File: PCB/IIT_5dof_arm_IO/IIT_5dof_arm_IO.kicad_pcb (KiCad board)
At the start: 2 copper layers, 60.5 x 0.5 mm, 48 parts, among them J15 Conn_01x03, J16 Conn_01x05, J2 Conn_02x03_Counter_Clockwise, J3 Conn_01x03, J4 Conn_01x04, J5 Conn_01x04, SW10 SW_Push, SW11 SW_Push, SW12 SW_Push, SW13 SW_Push, SW14 SW_Push, SW2 SW_Push, SW4 SW_Push, SW5 SW_Push, SW6 SW_Push, SW7 SW_Push, SW8 SW_Push, SW9 SW_Push, U6 ATmega328P-A, Y1 16MHz

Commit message: Split control board and I/O cards into separate projects
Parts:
- removed BZ1: Buzzer, Connector_Molex:Molex_KK-254_AE-6410-02A_1x02_P2.54mm_Vertical
- removed C10, C6, C7, C9: 100nF, Capacitor_SMD:C_0805_2012Metric_Pad1.18x1.45mm_HandSolder
- removed C2, C3: 22pF, Capacitor_SMD:C_0805_2012Metric_Pad1.18x1.45mm_HandSolder
- removed C4, C5: 1uF, Capacitor_SMD:C_0805_2012Metric_Pad1.18x1.45mm_HandSolder
- removed C8: 4.7uF, Capacitor_SMD:C_1206_3216Metric_Pad1.33x1.80mm_HandSolder
- removed D14: LED, LED_THT:LED_D5.0mm
- removed J15, J3: Conn_01x03, Connector_Molex:Molex_KK-254_AE-6410-03A_1x03_P2.54mm_Vertical
- removed J16: Conn_01x05, Connector_Molex:Molex_KK-254_AE-6410-05A_1x05_P2.54mm_Vertical
- removed J2: Conn_02x03_Counter_Clockwise, Connector_PinHeader_2.54mm:PinHeader_2x03_P2.54mm_Vertical
- removed J4, J5: Conn_01x04, Connector_Molex:Molex_KK-254_AE-6410-04A_1x04_P2.54mm_Vertical
- removed R20, R21, R22, R23, R24, R25, R26, R27, R28, R29, R30, R31, R35: 220, Resistor_SMD:R_0805_2012Metric_Pad1.20x1.40mm_HandSolder
- removed R32, R33, R34, R52: 10k, Resistor_SMD:R_0805_2012Metric_Pad1.20x1.40mm_HandSolder
- removed SW10, SW11, SW12, SW13, SW14, SW2, SW4, SW5, SW6, SW7, SW8, SW9: SW_Push, Connector_Molex:Molex_KK-254_AE-6410-02A_1x02_P2.54mm_Vertical
- removed U6: ATmega328P-A, Package_QFP:TQFP-32_7x7mm_P0.8mm
- removed Y1: 16MHz, Crystal:Crystal_SMD_HC49-SD_HandSoldering
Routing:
- net (no net): track 966.4 -> 0.00 mm, vias 16 -> 0
- removed copper zone on B.Cu, net (none)
- removed copper zone on F.Cu, net (none)
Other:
- board outline removed

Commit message: Organize schematic and generate initi PCB
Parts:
- added BZ1: Buzzer, Connector_Molex:Molex_KK-254_AE-6410-02A_1x02_P2.54mm_Vertical, F.Cu at (148.5, 46.3)
- added C1: 100nF, Capacitor_SMD:C_0805_2012Metric_Pad1.18x1.45mm_HandSolder, F.Cu at (160.5, 82.1)
- added C2: 10nF, Capacitor_SMD:C_0805_2012Metric_Pad1.18x1.45mm_HandSolder, F.Cu at (160.5, 85.2)
- added C3: 10nF, Capacitor_SMD:C_0805_2012Metric_Pad1.18x1.45mm_HandSolder, F.Cu at (160.5, 88.2)
- added C4: 10nF, Capacitor_SMD:C_0805_2012Metric_Pad1.18x1.45mm_HandSolder, F.Cu at (160.5, 91.2)
- added C5: 22pF, Capacitor_SMD:C_0805_2012Metric_Pad1.18x1.45mm_HandSolder, F.Cu at (160.5, 94.2)
- added C6: 22pF, Capacitor_SMD:C_0805_2012Metric_Pad1.18x1.45mm_HandSolder, F.Cu at (160.5, 97.2)
- added C7: 1uF, Capacitor_SMD:C_0805_2012Metric_Pad1.18x1.45mm_HandSolder, F.Cu at (160.5, 100.2)
- added C8: 4.7uF, Capacitor_SMD:C_1206_3216Metric_Pad1.33x1.80mm_HandSolder, F.Cu at (178.9, 104.3)
- added C9: 1uF, Capacitor_SMD:C_0805_2012Metric_Pad1.18x1.45mm_HandSolder, F.Cu at (160.5, 103.2)
- added D13: D, Diode_SMD:D_0805_2012Metric_Pad1.15x1.40mm_HandSolder, F.Cu at (142.9, 91.0)
- added D14: LED, Connector_Molex:Molex_KK-254_AE-6410-02A_1x02_P2.54mm_Vertical, F.Cu at (155.6, 46.3)
- added J1: Conn_01x05, Connector_Molex:Molex_KK-254_AE-6410-05A_1x05_P2.54mm_Vertical, F.Cu at (131.2, 105.0)
- added J10: Conn_01x06, Connector_Molex:Molex_KK-254_AE-6410-06A_1x06_P2.54mm_Vertical, F.Cu at (58.5, 42.1)
- added J11: Conn_01x06, Connector_Molex:Molex_KK-254_AE-6410-06A_1x06_P2.54mm_Vertical, F.Cu at (58.5, 49.9)
- added J12: Conn_01x06, Connector_Molex:Molex_KK-254_AE-6410-06A_1x06_P2.54mm_Vertical, F.Cu at (58.5, 57.8)
- added J13: Conn_01x06, Connector_Molex:Molex_KK-254_AE-6410-06A_1x06_P2.54mm_Vertical, F.Cu at (58.5, 65.6)
- added J2: Conn_01x03, Connector_Molex:Molex_KK-254_AE-6410-03A_1x03_P2.54mm_Vertical, F.Cu at (177.5, 84.6)
- added J3: Conn_02x03_Counter_Clockwise, Connector_PinHeader_2.54mm:PinHeader_2x03_P2.54mm_Vertical, F.Cu at (179.5, 68.2)
- added J4: Conn_01x03, Connector_Molex:Molex_KK-254_AE-6410-03A_1x03_P2.54mm_Vertical, F.Cu at (177.5, 92.4)
- added J5: Conn_01x04, Connector_Molex:Molex_KK-254_AE-6410-04A_1x04_P2.54mm_Vertical, F.Cu at (165.2, 84.6)
- added J6: Conn_01x04, Connector_Molex:Molex_KK-254_AE-6410-04A_1x04_P2.54mm_Vertical, F.Cu at (165.2, 92.4)
- added J7: Conn_02x13_Top_Bottom, Connector_IDC:IDC-Header_2x13_P2.54mm_Vertical, F.Cu at (27.0, 56.9)
- added J8: Conn_01x06, Connector_Molex:Molex_KK-254_AE-6410-06A_1x06_P2.54mm_Vertical, F.Cu at (58.5, 26.4)
- added J9: Conn_01x06, Connector_Molex:Molex_KK-254_AE-6410-06A_1x06_P2.54mm_Vertical, F.Cu at (58.5, 34.2)
- added Q1: 2N7002, Package_TO_SOT_SMD:SOT-23, F.Cu at (179.6, 78.0)
- added R1: 10k, Resistor_SMD:R_0805_2012Metric_Pad1.20x1.40mm_HandSolder, F.Cu at (160.5, 67.4)
- added R10: 220, Resistor_SMD:R_0805_2012Metric_Pad1.20x1.40mm_HandSolder, F.Cu at (165.3, 79.2)
- added R11: 220, Resistor_SMD:R_0805_2012Metric_Pad1.20x1.40mm_HandSolder, F.Cu at (170.0, 67.4)
- added R12: 220, Resistor_SMD:R_0805_2012Metric_Pad1.20x1.40mm_HandSolder, F.Cu at (170.0, 70.3)
- added R13: 220, Resistor_SMD:R_0805_2012Metric_Pad1.20x1.40mm_HandSolder, F.Cu at (170.0, 73.3)
- added R14: 220, Resistor_SMD:R_0805_2012Metric_Pad1.20x1.40mm_HandSolder, F.Cu at (170.0, 76.2)
- added R15: 10k, Resistor_SMD:R_0805_2012Metric_Pad1.20x1.40mm_HandSolder, F.Cu at (170.0, 79.2)
- added R16: 10k, Resistor_SMD:R_0805_2012Metric_Pad1.20x1.40mm_HandSolder, F.Cu at (174.8, 67.4)
- added R17: 160, Resistor_SMD:R_0805_2012Metric_Pad1.20x1.40mm_HandSolder, F.Cu at (174.8, 70.3)
- added R18: 100k, Resistor_SMD:R_0805_2012Metric_Pad1.20x1.40mm_HandSolder, F.Cu at (174.8, 73.3)
- added R19: 160, Resistor_SMD:R_0805_2012Metric_Pad1.20x1.40mm_HandSolder, F.Cu at (174.8, 76.2)
- added R2: 10k, Resistor_SMD:R_0805_2012Metric_Pad1.20x1.40mm_HandSolder, F.Cu at (160.5, 70.3)
- added R20: 220, Resistor_SMD:R_0805_2012Metric_Pad1.20x1.40mm_HandSolder, F.Cu at (174.8, 79.2)
- added R3: 220, Resistor_SMD:R_0805_2012Metric_Pad1.20x1.40mm_HandSolder, F.Cu at (160.5, 73.3)
- added R4: 220, Resistor_SMD:R_0805_2012Metric_Pad1.20x1.40mm_HandSolder, F.Cu at (160.5, 76.2)
- added R5: 220, Resistor_SMD:R_0805_2012Metric_Pad1.20x1.40mm_HandSolder, F.Cu at (160.5, 79.2)
- added R6: 220, Resistor_SMD:R_0805_2012Metric_Pad1.20x1.40mm_HandSolder, F.Cu at (165.3, 67.4)
- added R7: 220, Resistor_SMD:R_0805_2012Metric_Pad1.20x1.40mm_HandSolder, F.Cu at (165.3, 70.3)
- added R8: 220, Resistor_SMD:R_0805_2012Metric_Pad1.20x1.40mm_HandSolder, F.Cu at (165.3, 73.3)
- added R9: 220, Resistor_SMD:R_0805_2012Metric_Pad1.20x1.40mm_HandSolder, F.Cu at (165.3, 76.2)
- added SW1: SW_Push, Connector_Molex:Molex_KK-254_AE-6410-02A_1x02_P2.54mm_Vertical, F.Cu at (162.7, 46.3)
- added SW10: SW_Push, Connector_Molex:Molex_KK-254_AE-6410-02A_1x02_P2.54mm_Vertical, F.Cu at (177.0, 54.1)
- added SW11: SW_Push, Connector_Molex:Molex_KK-254_AE-6410-02A_1x02_P2.54mm_Vertical, F.Cu at (148.5, 62.0)
- added SW12: SW_Push, Connector_Molex:Molex_KK-254_AE-6410-02A_1x02_P2.54mm_Vertical, F.Cu at (155.6, 62.0)
- added SW13: SW_Push, Connector_Molex:Molex_KK-254_AE-6410-02A_1x02_P2.54mm_Vertical, F.Cu at (162.7, 62.0)
- added SW14: SW_Push, Connector_Molex:Molex_KK-254_AE-6410-02A_1x02_P2.54mm_Vertical, F.Cu at (169.8, 62.0)
- added SW2: SW_Push, Connector_Molex:Molex_KK-254_AE-6410-02A_1x02_P2.54mm_Vertical, F.Cu at (169.8, 46.3)
- added SW3: SW_Push, Connector_Molex:Molex_KK-254_AE-6410-02A_1x02_P2.54mm_Vertical, F.Cu at (177.0, 46.3)
- added SW4: SW_Push, Connector_Molex:Molex_KK-254_AE-6410-02A_1x02_P2.54mm_Vertical, F.Cu at (148.5, 54.1)
- added SW5: SW_Push, Connector_Molex:Molex_KK-254_AE-6410-02A_1x02_P2.54mm_Vertical, F.Cu at (155.6, 54.1)
- added SW6: SW_Push, Connector_Molex:Molex_KK-254_AE-6410-02A_1x02_P2.54mm_Vertical, F.Cu at (162.7, 54.1)
- added SW8: SW_Push, Button_Switch_SMD:SW_SPST_FSMSM, F.Cu at (169.4, 105.1)
- added SW9: SW_Push, Connector_Molex:Molex_KK-254_AE-6410-02A_1x02_P2.54mm_Vertical, F.Cu at (169.8, 54.1)
- added U1: ATmega328P-A, Package_QFP:TQFP-32_7x7mm_P0.8mm, F.Cu at (134.7, 95.3)
- added Y1: 16MHz, Crystal:Crystal_SMD_HC49-SD_HandSoldering, F.Cu at (173.7, 99.5)
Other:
- board outline added: 100 x 100 mm

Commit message: PCB layout
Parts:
- removed J10, J11, J12, J13, J8, J9: Conn_01x06, Connector_Molex:Molex_KK-254_AE-6410-06A_1x06_P2.54mm_Vertical
- removed J7: Conn_02x13_Top_Bottom, Connector_IDC:IDC-Header_2x13_P2.54mm_Vertical
- added C10: 0.33uF, Capacitor_SMD:C_0805_2012Metric_Pad1.18x1.45mm_HandSolder, F.Cu at (91.4, 52.3)
- added C11: 0.047uF, Capacitor_SMD:C_0805_2012Metric_Pad1.18x1.45mm_HandSolder, F.Cu at (95.7, 52.3)
- added C12: 0.1uF, Capacitor_SMD:C_0805_2012Metric_Pad1.18x1.45mm_HandSolder, B.Cu at (95.7, 70.8)
- added C13: 0.33uF, Capacitor_SMD:C_0805_2012Metric_Pad1.18x1.45mm_HandSolder, B.Cu at (94.5, 52.4)
- added C14: 0.33uF, Capacitor_SMD:C_0805_2012Metric_Pad1.18x1.45mm_HandSolder, F.Cu at (87.9, 52.1)
- added C15: 10nF, Capacitor_SMD:C_0805_2012Metric_Pad1.18x1.45mm_HandSolder, B.Cu at (104.1, 34.3)
- added C16: 10nF, Capacitor_SMD:C_0805_2012Metric_Pad1.18x1.45mm_HandSolder, B.Cu at (92.5, 34.3)
- added C17: 10nF, Capacitor_SMD:C_0805_2012Metric_Pad1.18x1.45mm_HandSolder, B.Cu at (80.5, 34.0)
- added C18: 10nF, Capacitor_SMD:C_0805_2012Metric_Pad1.18x1.45mm_HandSolder, B.Cu at (68.1, 34.0)
- added C19: 10nF, Capacitor_SMD:C_0805_2012Metric_Pad1.18x1.45mm_HandSolder, B.Cu at (55.5, 34.3)
- added C20: 10nF, Capacitor_SMD:C_0805_2012Metric_Pad1.18x1.45mm_HandSolder, B.Cu at (59.4, 86.1)
- added C21: 10nF, Capacitor_SMD:C_0805_2012Metric_Pad1.18x1.45mm_HandSolder, B.Cu at (64.3, 90.5)
- added C22: 10nF, Capacitor_SMD:C_0805_2012Metric_Pad1.18x1.45mm_HandSolder, B.Cu at (84.6, 90.5)
- added C23: 10nF, Capacitor_SMD:C_0805_2012Metric_Pad1.18x1.45mm_HandSolder, B.Cu at (96.7, 90.5)
- added C24: 10nF, Capacitor_SMD:C_0805_2012Metric_Pad1.18x1.45mm_HandSolder, B.Cu at (108.6, 90.5)
- added C25: 10nF, Capacitor_SMD:C_0805_2012Metric_Pad1.18x1.45mm_HandSolder, F.Cu at (32.1, 38.6)
- added C26: 10nF, Capacitor_SMD:C_0805_2012Metric_Pad1.18x1.45mm_HandSolder, F.Cu at (34.3, 86.1)
- added D1: LED, Connector_Molex:Molex_KK-254_AE-6410-02A_1x02_P2.54mm_Vertical, F.Cu at (99.3, 25.1)
- added D10: LED, Connector_Molex:Molex_KK-254_AE-6410-02A_1x02_P2.54mm_Vertical, F.Cu at (68.8, 99.5)
- added D11: LED, Connector_Molex:Molex_KK-254_AE-6410-02A_1x02_P2.54mm_Vertical, F.Cu at (53.7, 99.5)
- added D12: LED, Connector_Molex:Molex_KK-254_AE-6410-02A_1x02_P2.54mm_Vertical, F.Cu at (41.4, 99.5)
- added D15: SMAJ12A, Diode_SMD:D_SMA, B.Cu at (100.2, 71.8)
- added D16: SMAJ12A, Diode_SMD:D_SMA, F.Cu at (104.4, 71.7)
- added D17: SMAJ12A, Diode_SMD:D_SMA, F.Cu at (104.2, 63.8)
- added D2: LED, Connector_Molex:Molex_KK-254_AE-6410-02A_1x02_P2.54mm_Vertical, F.Cu at (87.3, 25.1)
- added D3: LED, Connector_Molex:Molex_KK-254_AE-6410-02A_1x02_P2.54mm_Vertical, F.Cu at (75.7, 25.1)
- added D4: LED, Connector_Molex:Molex_KK-254_AE-6410-02A_1x02_P2.54mm_Vertical, F.Cu at (63.4, 25.1)
- added D5: LED, Connector_Molex:Molex_KK-254_AE-6410-02A_1x02_P2.54mm_Vertical, F.Cu at (50.8, 25.1)
- added D6: LED, Connector_Molex:Molex_KK-254_AE-6410-02A_1x02_P2.54mm_Vertical, F.Cu at (37.0, 25.0)
- added D7: LED, Connector_Molex:Molex_KK-254_AE-6410-02A_1x02_P2.54mm_Vertical, F.Cu at (104.0, 99.5)
- added D8: LED, Connector_Molex:Molex_KK-254_AE-6410-02A_1x02_P2.54mm_Vertical, F.Cu at (92.0, 99.5)
- added D9: LED, Connector_Molex:Molex_KK-254_AE-6410-02A_1x02_P2.54mm_Vertical, F.Cu at (80.0, 99.5)
- added F1: 1812L050PR, IIT_5dof_arm_IO:1812L050PR__1.78mm_3.15mm_3.45mm, B.Cu at (104.5, 72.4)
- added G***: LOGO, IIT_5dof_arm:IIT_logo_15x15mm, F.Cu at (42.2, 71.6)
- added H1: MountingHole, MountingHole:MountingHole_3.2mm_M3, F.Cu at (24.0, 24.0)
- added H2: MountingHole, MountingHole:MountingHole_3.2mm_M3, F.Cu at (116.0, 24.0)
- added H3: MountingHole, MountingHole:MountingHole_3.2mm_M3, F.Cu at (24.0, 101.0)
- added H4: MountingHole, MountingHole:MountingHole_3.2mm_M3, F.Cu at (116.0, 101.0)
- added Q2: 2N7002, Package_TO_SOT_SMD:SOT-23, F.Cu at (37.1, 33.4)
- added Q3: 2N7002, Package_TO_SOT_SMD:SOT-23, B.Cu at (53.6, 91.2)
- added Q4: 2N7002, Package_TO_SOT_SMD:SOT-23, F.Cu at (41.3, 91.2)
- added R21: 4.7k, Resistor_SMD:R_0805_2012Metric_Pad1.20x1.40mm_HandSolder, B.Cu at (90.1, 67.9)
- added R22: 4.7k, Resistor_SMD:R_0805_2012Metric_Pad1.20x1.40mm_HandSolder, B.Cu at (90.1, 64.4)
- added R23: 10k, Resistor_SMD:R_0805_2012Metric_Pad1.20x1.40mm_HandSolder, F.Cu at (29.5, 50.6)
- added R24: 10k, Resistor_SMD:R_0805_2012Metric_Pad1.20x1.40mm_HandSolder, B.Cu at (104.1, 29.6)
- added R25: 10k, Resistor_SMD:R_0805_2012Metric_Pad1.20x1.40mm_HandSolder, B.Cu at (92.5, 29.6)
- added R26: 10k, Resistor_SMD:R_0805_2012Metric_Pad1.20x1.40mm_HandSolder, B.Cu at (80.5, 29.4)
- added R27: 10k, Resistor_SMD:R_0805_2012Metric_Pad1.20x1.40mm_HandSolder, B.Cu at (68.1, 29.5)
- added R28: 10k, Resistor_SMD:R_0805_2012Metric_Pad1.20x1.40mm_HandSolder, B.Cu at (55.5, 29.7)
- added R29: 10k, Resistor_SMD:R_0805_2012Metric_Pad1.20x1.40mm_HandSolder, F.Cu at (33.2, 29.3)
- added R31: 10k, Resistor_SMD:R_0805_2012Metric_Pad1.20x1.40mm_HandSolder, B.Cu at (108.6, 95.0)
- added R32: 10k, Resistor_SMD:R_0805_2012Metric_Pad1.20x1.40mm_HandSolder, B.Cu at (96.7, 95.0)
- added R33: 10k, Resistor_SMD:R_0805_2012Metric_Pad1.20x1.40mm_HandSolder, B.Cu at (84.6, 95.0)
- added R34: 10k, Resistor_SMD:R_0805_2012Metric_Pad1.20x1.40mm_HandSolder, B.Cu at (50.2, 95.5)
- added R35: 10k, Resistor_SMD:R_0805_2012Metric_Pad1.20x1.40mm_HandSolder, F.Cu at (45.3, 95.5)
- added R37: 10k, Resistor_SMD:R_0805_2012Metric_Pad1.20x1.40mm_HandSolder, B.Cu at (64.3, 95.0)
- added SW15: SW_SPDT, Connector_PinHeader_2.54mm:PinHeader_1x03_P2.54mm_Vertical, F.Cu at (25.0, 47.1)
- added U2: MAX3232, Package_SO:SOIC-16W_5.3x10.2mm_P1.27mm, F.Cu at (91.3, 60.2)
- C4, D13, Q1, R1, R13, R17, R18, R20: moved to B.Cu
- J6: value Conn_01x04 -> DE9_Plug_MountingHoles; footprint Connector_Molex:Molex_KK-254_AE-6410-04A_1x04_P2.54mm_Vertical -> Connector_Dsub:DSUB-9_Male_Horizontal_P2.77x2.84mm_EdgePinOffset7.70mm_Housed_MountingHolesOffset9.12mm
- moved J3 150.1 mm to (29.6, 76.2), turned to -90 degrees
- moved SW8 150.0 mm to (25.1, 64.4), turned to 90 degrees
- moved R19 140.5 mm to (35.5, 57.3), turned to -90 degrees
- moved R15 139.7 mm to (30.7, 68.9)
- moved R8 135.6 mm to (37.0, 29.4), turned to -90 degrees
- moved Q1 132.5 mm to (48.0, 62.6), turned to 180 degrees
- moved SW14 131.9 mm to (40.3, 87.1), turned to 90 degrees
- moved R14 130.2 mm to (41.3, 95.5), turned to 90 degrees
- moved SW6 125.5 mm to (38.0, 40.0), turned to 90 degrees
- moved J2 123.4 mm to (54.5, 73.9), turned to -90 degrees
- moved R18 122.7 mm to (52.5, 62.8), turned to -90 degrees
- moved R7 121.6 mm to (50.9, 29.1), turned to -90 degrees
- moved Y1 120.6 mm to (64.6, 48.1)
- moved R17 118.8 mm to (56.3, 61.9), turned to 180 degrees
- moved R13 118.4 mm to (53.7, 95.5), turned to 90 degrees
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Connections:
- J3 pad 1: /UIPanel_BUTT5A__UIPanel_Prog_MISO -> /UIPanel_BUTT6A__UIPanel_Prog_MOSI
- J3 pad 2: /UIPanel_BUTT6A__UIPanel_Prog_SCK -> /UIPanel_BUTT6B__UIPanel_Prog_MISO
- J3 pad 4: UIPanel_GND -> /UIPanel_BUTT5B__UIPanel_Prog_SCK
- J3 pad 5: /UIPanel_BUTT4A__UIPanel_Prog_MOSI -> UIPanel_+5V
- J3 pad 6: UIPanel_+5V -> UIPanel_GND
- J6 pad 1: UIPanel_+5V -> Net-(F1-Pad1)
- J6 pad 2: /UIPanel_RX -> /RS232_RX
- J6 pad 3: /UIPanel_TX -> /RS232_TX
- J6 pad 4: UIPanel_GND -> unconnected-(J6-Pad4)
- R10 pad 1: /UIPanel_BUTT2B -> Net-(D8-K)
- R10 pad 2: UIPanel_GND -> /UIPanel_BUTT2B
- R11 pad 1: /UIPanel_BUTT3B -> Net-(D9-K)
- R11 pad 2: UIPanel_GND -> /UIPanel_BUTT3B
- R12 pad 1: /UIPanel_BUTT4B -> Net-(D10-K)
- R12 pad 2: UIPanel_GND -> /UIPanel_BUTT4B
- R13 pad 1: /UIPanel_BUTT5B -> Net-(D11-K)
- R13 pad 2: UIPanel_GND -> Net-(Q3-D)
- R14 pad 1: /UIPanel_BUTT6B -> Net-(D12-K)
- R14 pad 2: UIPanel_GND -> Net-(Q4-D)
- R3 pad 1: UIPanel_GND -> Net-(D1-K)
- R4 pad 1: UIPanel_GND -> Net-(D2-K)
- R5 pad 1: UIPanel_GND -> Net-(D3-K)
- R6 pad 1: UIPanel_GND -> Net-(D4-K)
- R6 pad 2: /UIPanel_BUTT4A__UIPanel_Prog_MOSI -> /UIPanel_BUTT4A
- R7 pad 1: UIPanel_GND -> Net-(D5-K)
- R7 pad 2: /UIPanel_BUTT5A__UIPanel_Prog_MISO -> /UIPanel_BUTT5A
- R8 pad 1: UIPanel_GND -> Net-(D6-K)
- R8 pad 2: /UIPanel_BUTT6A__UIPanel_Prog_SCK -> Net-(Q2-D)
- R9 pad 1: /UIPanel_BUTT1B -> Net-(D7-K)
- R9 pad 2: UIPanel_GND -> /UIPanel_BUTT1B
- SW1 pad 1: Net-(SW1-Pad1) -> UIPanel_GND
- SW10 pad 1: Net-(SW10-Pad1) -> /UIPanel_BUTT2B
- SW10 pad 2: /UIPanel_BUTT2B -> UIPanel_GND
- SW11 pad 1: Net-(SW11-Pad1) -> /UIPanel_BUTT3B
- SW11 pad 2: /UIPanel_BUTT3B -> UIPanel_GND
- SW12 pad 1: Net-(SW12-Pad1) -> /UIPanel_BUTT4B
- SW12 pad 2: /UIPanel_BUTT4B -> UIPanel_GND
- SW13 pad 1: Net-(SW13-Pad1) -> /UIPanel_BUTT5B__UIPanel_Prog_SCK
- SW13 pad 2: /UIPanel_BUTT5B -> UIPanel_GND
- SW14 pad 1: Net-(SW14-Pad1) -> /UIPanel_BUTT6B__UIPanel_Prog_MISO
- SW14 pad 2: /UIPanel_BUTT6B -> UIPanel_GND
- SW2 pad 1: Net-(SW2-Pad1) -> UIPanel_GND
- SW3 pad 1: Net-(SW3-Pad1) -> UIPanel_GND
- SW4 pad 1: Net-(SW4-Pad1) -> UIPanel_GND
- SW4 pad 2: /UIPanel_BUTT4A__UIPanel_Prog_MOSI -> /UIPanel_BUTT4A
- SW5 pad 1: Net-(SW5-Pad1) -> UIPanel_GND
- SW5 pad 2: /UIPanel_BUTT5A__UIPanel_Prog_MISO -> /UIPanel_BUTT5A
- SW6 pad 1: Net-(SW6-Pad1) -> UIPanel_GND
- SW6 pad 2: /UIPanel_BUTT6A__UIPanel_Prog_SCK -> /UIPanel_BUTT6A__UIPanel_Prog_MOSI
- SW9 pad 1: Net-(SW9-Pad1) -> /UIPanel_BUTT1B
- SW9 pad 2: /UIPanel_BUTT1B -> UIPanel_GND
- U1 pad 10: /UIPanel_Enc_BUTT -> /UIPanel_BUTT2A
- U1 pad 11: /UIPanel_Buzz -> /UIPanel_BUTT3A
- U1 pad 12: /UIPanel_BUTT1A -> /UIPanel_BUTT4A
- U1 pad 13: /UIPanel_BUTT2A -> /UIPanel_BUTT5A
- U1 pad 14: /UIPanel_BUTT3A -> /UIPanel_Buzz
- U1 pad 15: /UIPanel_BUTT4A__UIPanel_Prog_MOSI -> /UIPanel_BUTT6A__UIPanel_Prog_MOSI
- U1 pad 16: /UIPanel_BUTT5A__UIPanel_Prog_MISO -> /UIPanel_BUTT6B__UIPanel_Prog_MISO
- U1 pad 17: /UIPanel_BUTT6A__UIPanel_Prog_SCK -> /UIPanel_BUTT5B__UIPanel_Prog_SCK
- U1 pad 2: /UIPanel_BUTT5B -> /UIPanel_Enc_BUTT
- U1 pad 23: /UIPanel_BUTT1B -> /UIPanel_BUTT4B
- U1 pad 24: /UIPanel_BUTT2B -> /UIPanel_BUTT3B
- U1 pad 25: /UIPanel_BUTT3B -> /UIPanel_BUTT2B
- U1 pad 26: /UIPanel_BUTT4B -> /UIPanel_BUTT1B
- U1 pad 9: /UIPanel_BUTT6B -> /UIPanel_BUTT1A
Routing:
- net UIPanel_+5V: track 0.00 -> 483.6 mm, vias 0 -> 2
- net /PROG_SW: track 0.00 -> 90.5 mm, vias 0 -> 2
- net /UIPanel_BUTT1A: track 0.00 -> 84.1 mm
- net /UIPanel_BUTT6A__UIPanel_Prog_MOSI: track 0.00 -> 81.2 mm
- net /UIPanel_BUTT2A: track 0.00 -> 74.1 mm
- net /UIPanel_BUTT5B__UIPanel_Prog_SCK: track 0.00 -> 67.6 mm
- net /UIPanel_BUTT3A: track 0.00 -> 64.1 mm
- net /UIPanel_BUTT6B__UIPanel_Prog_MISO: track 0.00 -> 61.8 mm, vias 0 -> 1
- net /UIPanel_reset: track 0.00 -> 60.0 mm, vias 0 -> 2
- net /UIPanel_Enc_BUTT: track 0.00 -> 58.1 mm
- net /UIPanel_BUTT1B: track 0.00 -> 57.8 mm
- net /UIPanel_BUTT4A: track 0.00 -> 53.5 mm
- net /UIPanel_BUTT5A: track 0.00 -> 51.1 mm
- net /UIPanel_Enc_A: track 0.00 -> 50.2 mm
- net /UIPanel_BUTT2B: track 0.00 -> 49.6 mm
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- added copper zone on B.Cu, net UIPanel_GND
- added copper zone on F.Cu, net UIPanel_GND
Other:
- board size 100 x 100 mm -> 100 x 85 mm
- board text added: "+"
- board text added: "+5V"
- board text added: "A1"
- board text added: "A2"
- board text added: "BUTT"
- board text added: "ChA"
- board text added: "ChB"
- board text added: "GND"
- board text added: "Kalm & Mürb Teach-robot Wired remote control v1.0 András Izsó 2024"
- board text added: "MISO"
- board text added: "MOSI"
- board text added: "RESET"
- board text added: "RS232 (DTE): 1: +5V 6: X 2: RX 7: X 3: TX 8: X 4: X 9: X 5: GND"
- board text added: "SCK"
- board text added: "SCL"
- board text added: "SDA"

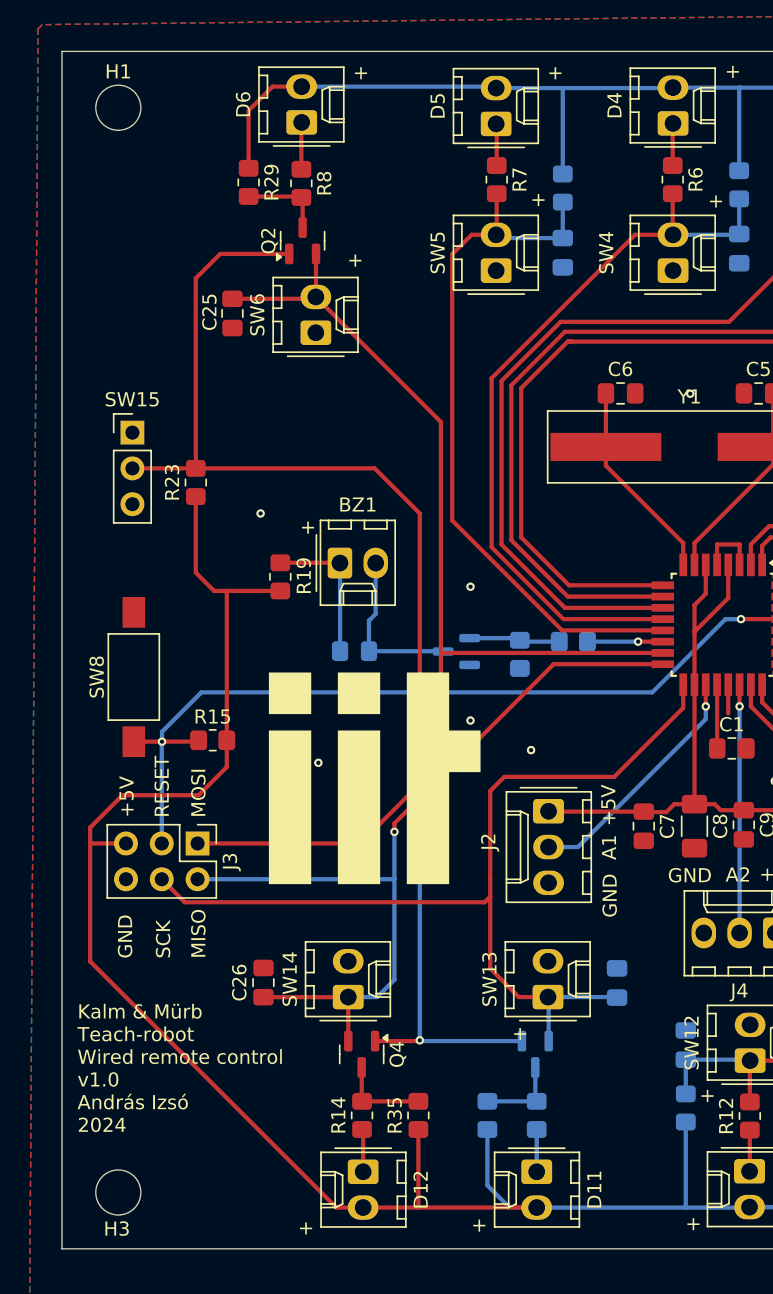
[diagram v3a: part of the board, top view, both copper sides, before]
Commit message: Fix SMAJ value, program pullup switch
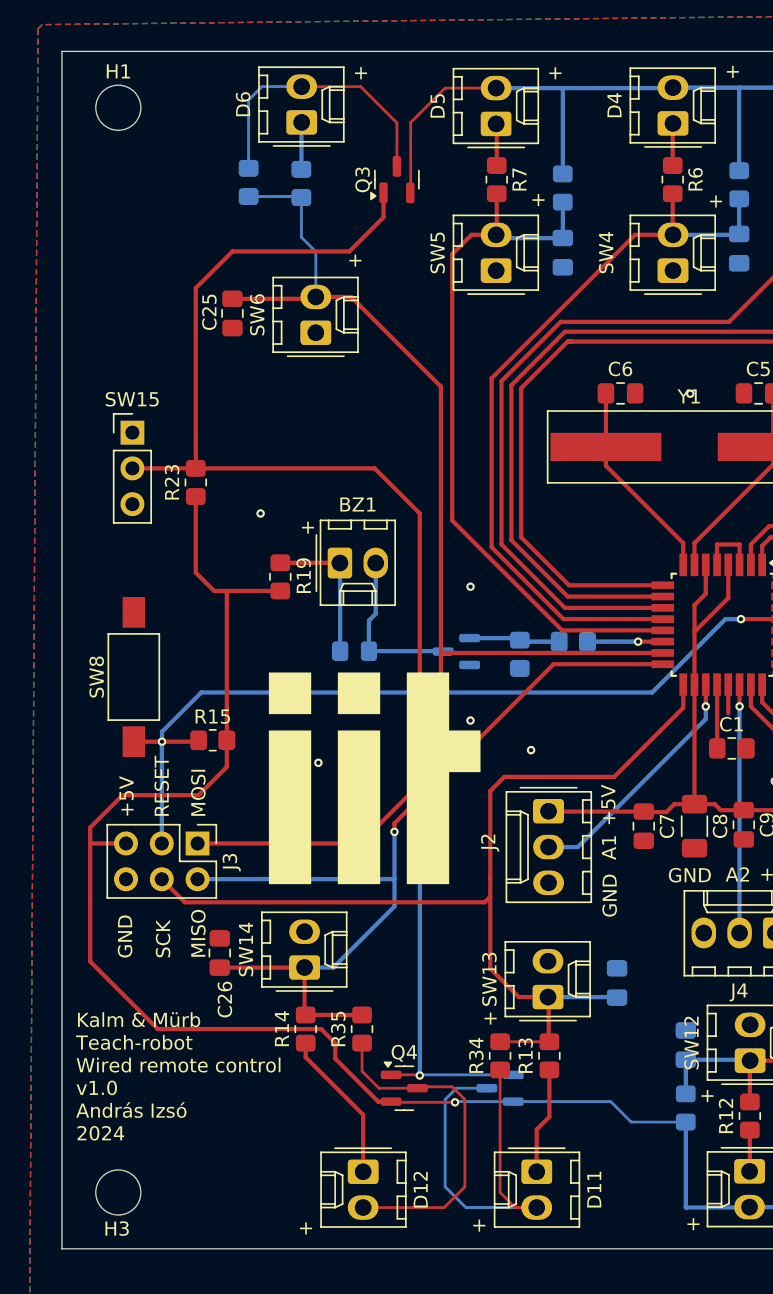
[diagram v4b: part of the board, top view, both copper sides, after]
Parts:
- D15: value SMAJ12A -> SMAJ5.0A
- Q2: value 2N7002 -> BSS84; moved to B.Cu
- Q3: value 2N7002 -> BSS84; moved to F.Cu
- Q4: value 2N7002 -> BSS84
- R13, R34: moved to F.Cu
- R29, R8: moved to B.Cu
- moved Q3 62.9 mm to (43.8, 29.1), turned to 90 degrees
- moved Q2 61.8 mm to (51.1, 93.6), turned to 180 degrees
- moved R14 7.32 mm to (37.3, 89.4)
- moved R35 7.32 mm to (41.3, 89.4)
- moved R13 4.32 mm to (54.6, 91.3)
- moved R34 4.32 mm to (51.1, 91.3)
- moved Q4 3.87 mm to (44.3, 93.6), turned to 0 degrees
- moved SW14 3.74 mm to (37.2, 85.0)
- moved C26 3.74 mm to (31.2, 84.0)
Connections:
- D11 pad 2: UIPanel_+5V -> Net-(D11-A)
- D12 pad 2: UIPanel_+5V -> Net-(D12-A)
- D6 pad 2: UIPanel_+5V -> Net-(D6-A)
- Q2 pad 2: /UIPanel_BUTT6A__UIPanel_Prog_MOSI -> UIPanel_+5V
- Q2 pad 3: Net-(Q2-D) -> Net-(D11-A)
- Q3 pad 2: /UIPanel_BUTT5B__UIPanel_Prog_SCK -> UIPanel_+5V
- Q3 pad 3: Net-(Q3-D) -> Net-(D6-A)
- Q4 pad 2: /UIPanel_BUTT6B__UIPanel_Prog_MISO -> UIPanel_+5V
- Q4 pad 3: Net-(Q4-D) -> Net-(D12-A)
- R13 pad 2: Net-(Q3-D) -> /UIPanel_BUTT5B__UIPanel_Prog_SCK
- R14 pad 2: Net-(Q4-D) -> /UIPanel_BUTT6B__UIPanel_Prog_MISO
- R29 pad 1: UIPanel_+5V -> Net-(D6-A)
- R29 pad 2: Net-(Q2-D) -> /UIPanel_BUTT6A__UIPanel_Prog_MOSI
- R34 pad 1: UIPanel_+5V -> Net-(D11-A)
- R34 pad 2: Net-(Q3-D) -> /UIPanel_BUTT5B__UIPanel_Prog_SCK
- R35 pad 1: UIPanel_+5V -> Net-(D12-A)
- R35 pad 2: Net-(Q4-D) -> /UIPanel_BUTT6B__UIPanel_Prog_MISO
- R8 pad 2: Net-(Q2-D) -> /UIPanel_BUTT6A__UIPanel_Prog_MOSI
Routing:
- net Net-(D11-A): track 0.00 -> 28.3 mm
- net UIPanel_+5V: track 483.6 -> 458.0 mm, vias 2 -> 3
- net Net-(D12-A): track 0.00 -> 24.2 mm
- net Net-(D6-A): track 0.00 -> 19.9 mm
- net /PROG_SW: track 90.5 -> 100.4 mm
- net /UIPanel_BUTT6A__UIPanel_Prog_MOSI: track 81.2 -> 90.8 mm
- net Net-(D12-K): track 3.03 -> 10.9 mm
- net Net-(Q4-D): track 6.41 -> 0.00 mm
- net Net-(Q2-D): track 5.94 -> 0.00 mm
- net Net-(Q3-D): track 5.94 -> 0.00 mm
- net Net-(D11-K): track 3.00 -> 7.60 mm
- net /UIPanel_BUTT5B__UIPanel_Prog_SCK: track 67.6 -> 71.1 mm
- net /UIPanel_BUTT6B__UIPanel_Prog_MISO: track 61.8 -> 65.2 mm
